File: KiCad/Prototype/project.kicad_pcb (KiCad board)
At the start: 2 copper layers, 166 x 70 mm, 75 parts, among them J1 Barrel_Jack, J10 POT 2, J11 POT 3, J12 POT 4, J13 POT 5, J14 PRESSURE, J15 MIDI IN, J16 MIDI OUT, J17 POT 6, J18 POT 7, J19 POT 8, J2 USB_B, J20 TTL MIDI, J3 ICSP, J4 BANK 0..7, J5 BANK 8..15, J6 EXPRESSION, J7 SUSTAIN, J8 PD6/ADC9/SPEAKER, J9 POT 1, Q1 PMV48XP,215, SW1 RESET, U1 74LS75, U10 HCPL-0600, U2 LMV358, U3 AMS1117-5.0, U4 ATMEGA32U4-AU, U5 74HC138, U6 74HC138, U7 74HC238, U8 74HC238, U9 74HC04, Y1 16 Mhz

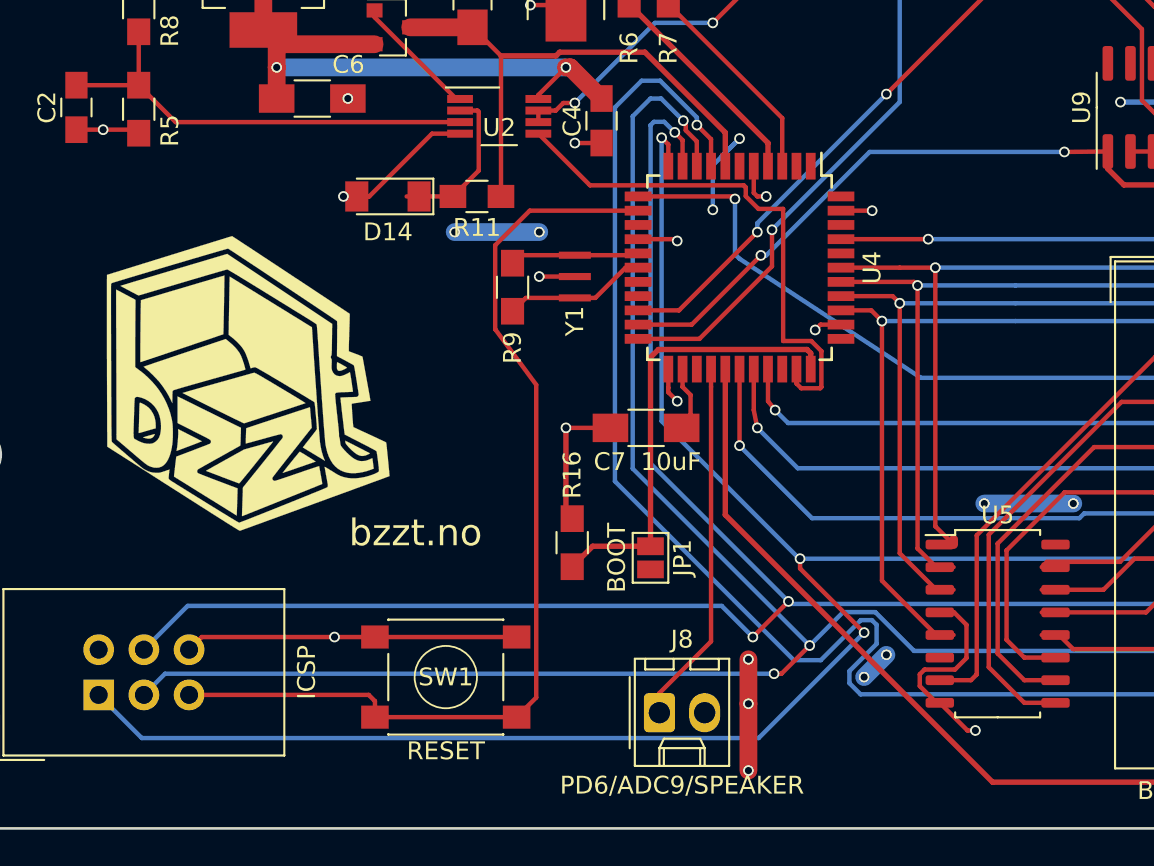
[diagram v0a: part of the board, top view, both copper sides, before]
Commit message: electrical changes for analog mux
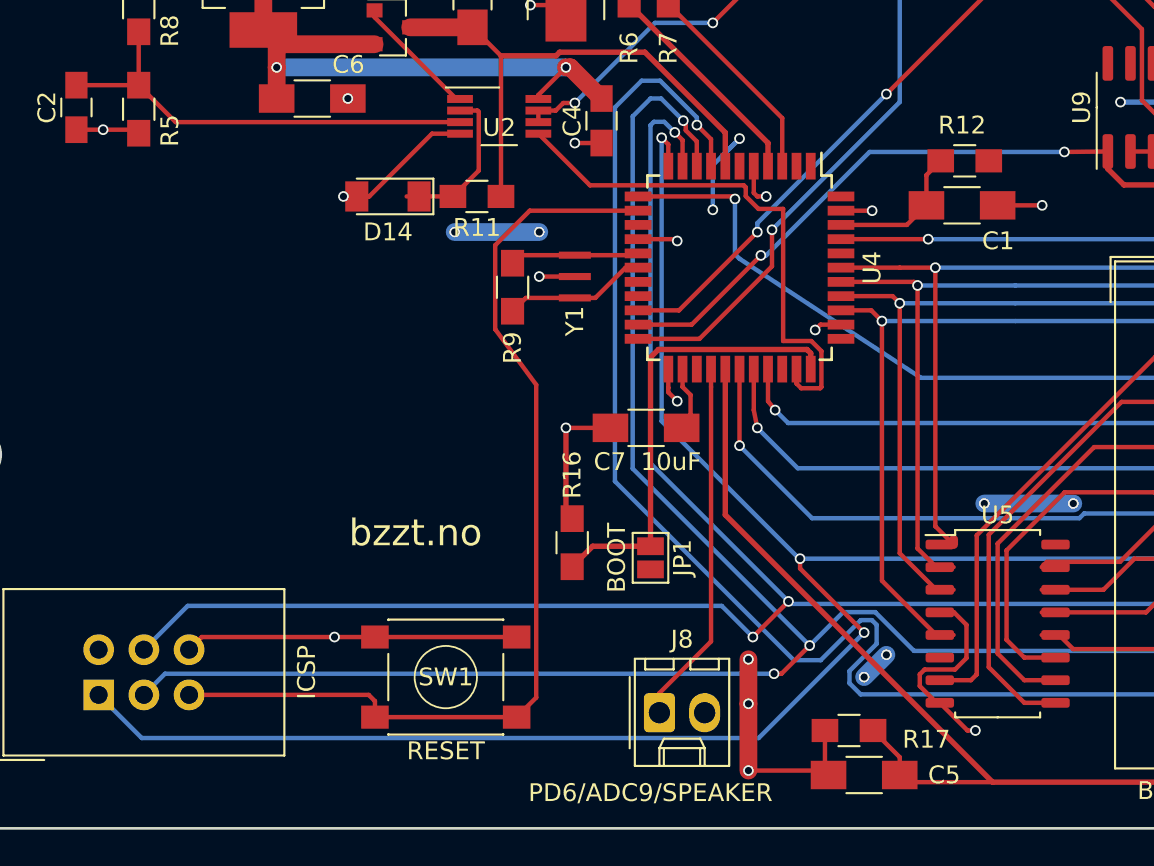
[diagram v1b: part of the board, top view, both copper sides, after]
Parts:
- removed G***: LOGO, footprints:bzzt-logo
- added C1: 10uF, footprints:C_1206_HandSoldering, F.Cu at (102.5, 75.0)
- added C5: 10uF, footprints:C_1206_HandSoldering, F.Cu at (97.0, 107.0)
- added R12: 1k, footprints:R_0805_HandSoldering, F.Cu at (102.7, 72.5)
- added R17: 1k, footprints:R_0805_HandSoldering, F.Cu at (96.2, 104.5)
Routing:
- net GND: track 143.0 -> 152.7 mm, vias 30 -> 31
- net /ADC10: track 236.1 -> 244.6 mm
- net /AREF: track 0.00 -> 8.09 mm
